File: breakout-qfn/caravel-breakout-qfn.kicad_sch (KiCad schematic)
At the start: 13 parts, among them CON1 REF-182665-01, CON2 REF-182665-01, CON3 73251-1352, U1 Caravel_QFN_TT4

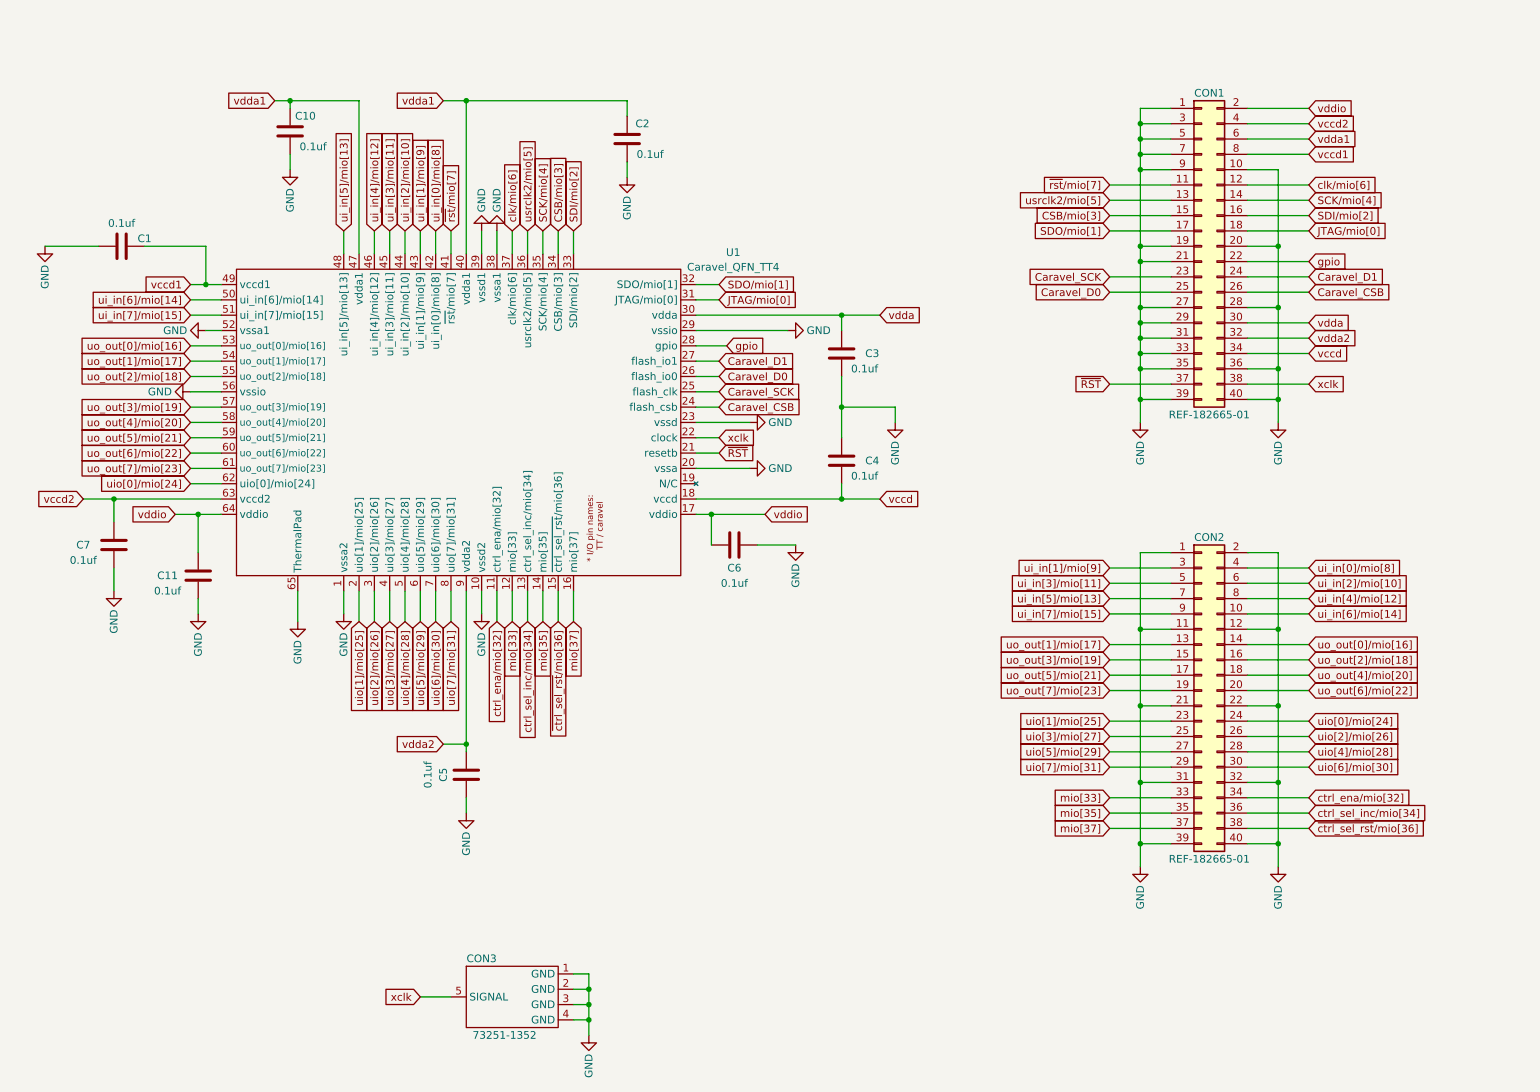
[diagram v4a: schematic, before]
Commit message: v3.0, breaking changes for ultra-goodness: EMC,TT pinout, FPGA
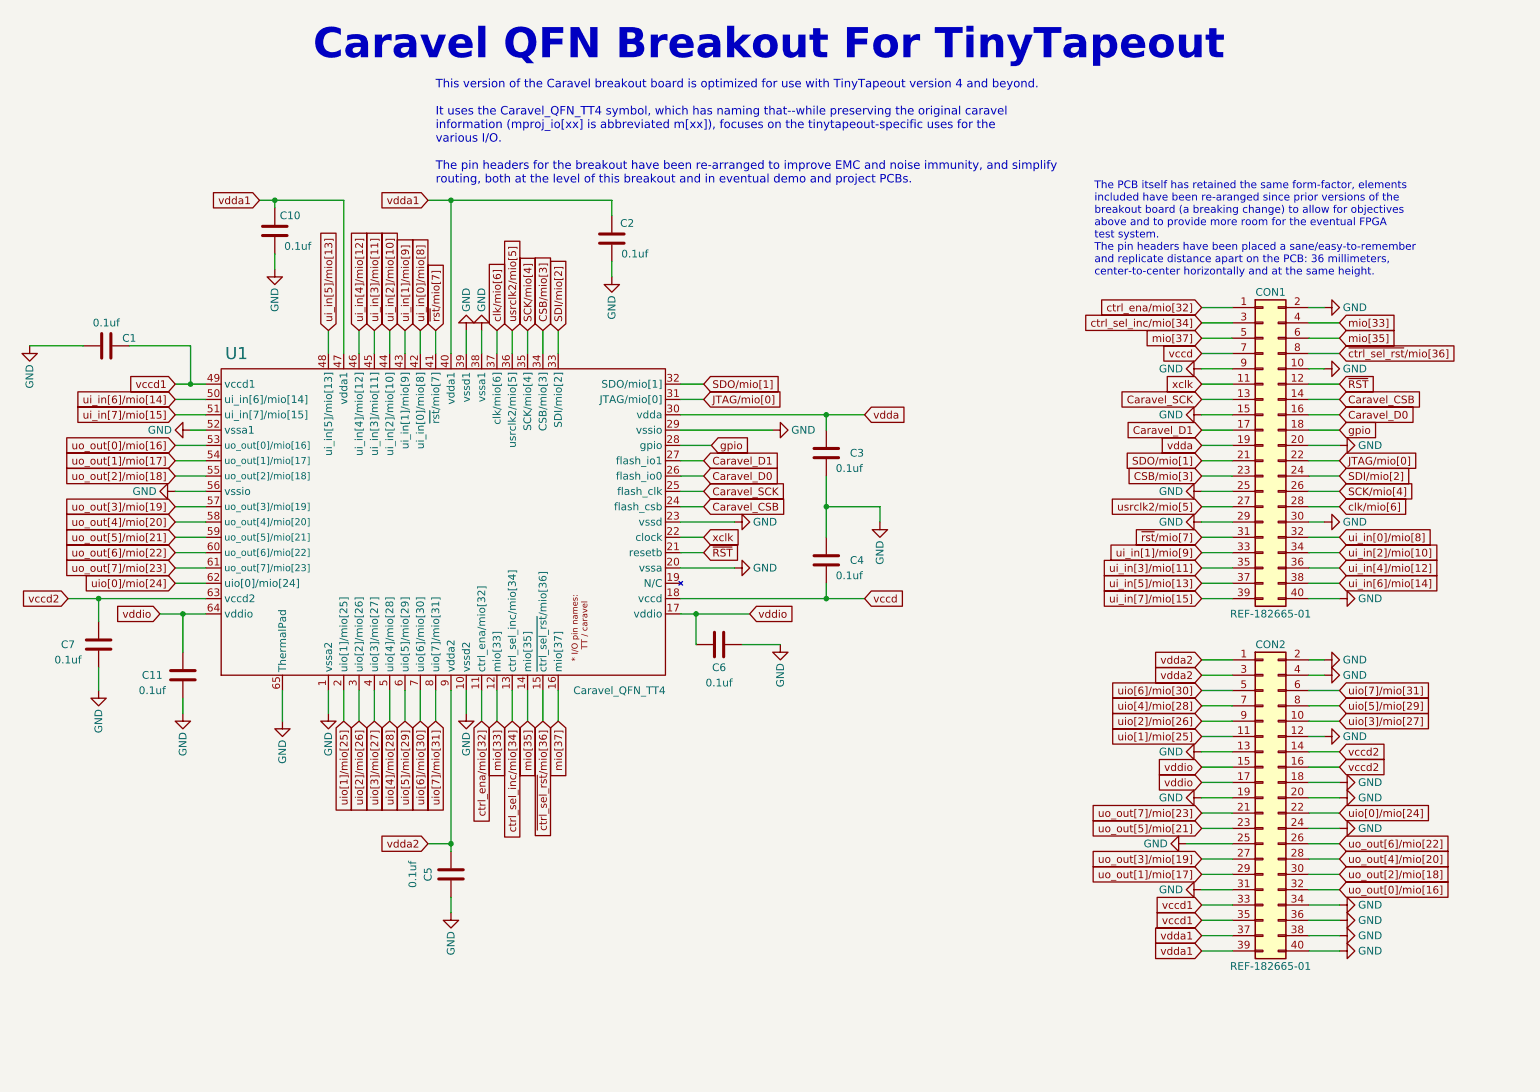
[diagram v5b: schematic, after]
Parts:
- removed CON3: 73251-1352, ok-connectors:TE_5-1814832-2, symbol ok-connectors:SMA_TH
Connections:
- net CSB/mio[3]: now also CON1.23 (Pin_23); no longer CON1.15 (Pin_15)
- net Caravel_CSB: now also CON1.14 (Pin_14); no longer CON1.26 (Pin_26)
- net Caravel_D0: now also CON1.16 (Pin_16); no longer CON1.25 (Pin_25)
- net Caravel_D1: now also CON1.17 (Pin_17); no longer CON1.24 (Pin_24)
- net Caravel_SCK: now also CON1.13 (Pin_13); no longer CON1.23 (Pin_23)
- net GND: now also CON1.15 (Pin_15), CON1.2 (Pin_2), CON1.25 (Pin_25), CON1.30 (Pin_30), CON2.13 (Pin_13), CON2.18 (Pin_18), CON2.19 (Pin_19), CON2.20 (Pin_20), CON2.24 (Pin_24), CON2.25 (Pin_25), CON2.34 (Pin_34), CON2.36 (Pin_36), CON2.38 (Pin_38), CON2.4 (Pin_4); no longer CON1.1 (Pin_1), CON1.19 (Pin_19), CON1.21 (Pin_21), CON1.27 (Pin_27), CON1.28 (Pin_28), CON1.3 (Pin_3), CON1.31 (Pin_31), CON1.33 (Pin_33), CON1.35 (Pin_35), CON1.36 (Pin_36), CON1.39 (Pin_39), CON1.5 (Pin_5), CON1.7 (Pin_7), CON2.1 (Pin_1), CON2.11 (Pin_11), CON2.21 (Pin_21), CON2.22 (Pin_22), CON2.32 (Pin_32), CON2.39 (Pin_39)
- net JTAG/mio[0]: now also CON1.22 (Pin_22); no longer CON1.18 (Pin_18)
- net SCK/mio[4]: now also CON1.26 (Pin_26); no longer CON1.14 (Pin_14)
- net SDI/mio[2]: now also CON1.24 (Pin_24); no longer CON1.16 (Pin_16)
- net SDO/mio[1]: now also CON1.21 (Pin_21); no longer CON1.17 (Pin_17)
- net clk/mio[6]: now also CON1.28 (Pin_28); no longer CON1.12 (Pin_12)
- net ctrl_ena/mio[32]: now also CON1.1 (Pin_1); no longer CON2.34 (Pin_34)
- net ctrl_sel_inc/mio[34]: now also CON1.3 (Pin_3); no longer CON2.36 (Pin_36)
- net gpio: now also CON1.18 (Pin_18); no longer CON1.22 (Pin_22)
- net mio[33]: now also CON1.4 (Pin_4); no longer CON2.33 (Pin_33)
- net mio[35]: now also CON1.6 (Pin_6); no longer CON2.35 (Pin_35)
- net mio[37]: now also CON1.5 (Pin_5); no longer CON2.37 (Pin_37)
- net ui_in[0]/mio[8]: now also CON1.32 (Pin_32); no longer CON2.4 (Pin_4)
- net ui_in[1]/mio[9]: now also CON1.33 (Pin_33); no longer CON2.3 (Pin_3)
- net ui_in[2]/mio[10]: now also CON1.34 (Pin_34); no longer CON2.6 (Pin_6)
- net ui_in[3]/mio[11]: now also CON1.35 (Pin_35); no longer CON2.5 (Pin_5)
- net ui_in[4]/mio[12]: now also CON1.36 (Pin_36); no longer CON2.8 (Pin_8)
- net ui_in[5]/mio[13]: now also CON1.37 (Pin_37); no longer CON2.7 (Pin_7)
- net ui_in[6]/mio[14]: now also CON1.38 (Pin_38); no longer CON2.10 (Pin_10)
- net ui_in[7]/mio[15]: now also CON1.39 (Pin_39); no longer CON2.9 (Pin_9)
- net uio[0]/mio[24]: now also CON2.22 (Pin_22); no longer CON2.24 (Pin_24)
- net uio[1]/mio[25]: now also CON2.11 (Pin_11); no longer CON2.23 (Pin_23)
- net uio[2]/mio[26]: now also CON2.9 (Pin_9); no longer CON2.26 (Pin_26)
- net uio[3]/mio[27]: now also CON2.10 (Pin_10); no longer CON2.25 (Pin_25)
- net uio[4]/mio[28]: now also CON2.7 (Pin_7); no longer CON2.28 (Pin_28)
- net uio[5]/mio[29]: now also CON2.8 (Pin_8); no longer CON2.27 (Pin_27)
- net uio[6]/mio[30]: now also CON2.5 (Pin_5); no longer CON2.30 (Pin_30)
- net uio[7]/mio[31]: now also CON2.6 (Pin_6); no longer CON2.29 (Pin_29)
- net uo_out[0]/mio[16]: now also CON2.32 (Pin_32); no longer CON2.14 (Pin_14)
- net uo_out[1]/mio[17]: now also CON2.29 (Pin_29); no longer CON2.13 (Pin_13)
- net uo_out[2]/mio[18]: now also CON2.30 (Pin_30); no longer CON2.16 (Pin_16)
- net uo_out[3]/mio[19]: now also CON2.27 (Pin_27); no longer CON2.15 (Pin_15)
- net uo_out[4]/mio[20]: now also CON2.28 (Pin_28); no longer CON2.18 (Pin_18)
- net uo_out[5]/mio[21]: now also CON2.23 (Pin_23); no longer CON2.17 (Pin_17)
- net uo_out[6]/mio[22]: now also CON2.26 (Pin_26); no longer CON2.20 (Pin_20)
- net uo_out[7]/mio[23]: now also CON2.21 (Pin_21); no longer CON2.19 (Pin_19)
- net usrclk2/mio[5]: now also CON1.27 (Pin_27); no longer CON1.13 (Pin_13)
- net vccd: now also CON1.7 (Pin_7); no longer CON1.34 (Pin_34)
- net vccd1: now also CON2.33 (Pin_33), CON2.35 (Pin_35); no longer CON1.8 (Pin_8)
- net vccd2: now also CON2.14 (Pin_14), CON2.16 (Pin_16); no longer CON1.4 (Pin_4)
- net vdda: now also CON1.19 (Pin_19); no longer CON1.30 (Pin_30)
- net vdda1: now also CON2.37 (Pin_37), CON2.39 (Pin_39); no longer CON1.6 (Pin_6)
- net vdda2: now also CON2.1 (Pin_1), CON2.3 (Pin_3); no longer CON1.32 (Pin_32)
- net vddio: now also CON2.15 (Pin_15), CON2.17 (Pin_17); no longer CON1.2 (Pin_2)
- net xclk: now also CON1.11 (Pin_11); no longer CON1.38 (Pin_38)
- net ~{RST}: now also CON1.12 (Pin_12); no longer CON1.37 (Pin_37)
- net ~{ctrl_sel_rst}/mio[36]: now also CON1.8 (Pin_8); no longer CON2.38 (Pin_38)
- net ~{rst}/mio[7]: now also CON1.31 (Pin_31); no longer CON1.11 (Pin_11)
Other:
- note added: "Caravel QFN Breakout For TinyTapeout"
- note added: "The PCB itself has retained the same form-factor, elements included have been re-aranged since prior versions of the breakout board (a breaking change) to allow for objectives above and to provide more room for the eventual FPGA test system. The pin headers have been placed a sane/easy-to-remember and replicate distance apart on the PCB: 36 millimeters, center-to-center horizontally and at the sa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"
- note added: "This version of the Caravel breakout board is optimized for use with TinyTapeout version 4 and beyond. It uses the Caravel_QFN_TT4 symbol, which has naming that--while preserving the original caravel information (mproj_io[xx] is abbreviated m[xx]), focuses on the tinytapeout-specific uses for the various I/O. The pin headers for the breakout have been re-arranged to improve EMC and noise immunity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"
- company: (none) -> Psychogenic Technologies
- moved on the sheet: C1, C10, C11, C2, C3, C4, C5, C6, C7, CON1, CON2, U1

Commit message: Comments and cleanup
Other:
- note added: "Caravel CLK"
- note added: "Caravel CLK and ~{RST}"
- note added: "Caravel flash"
- note added: "Caravel ~{RST}"
- note added: "HK SPI"
- note added: "Inputs"
- note added: "MUX Control"
- note added: "Project CLK"
- note added: "Project ~{RST}"
- note added: "This version of the Caravel breakout board is optimized for use with TinyTapeout version 4 and beyond. It uses the Caravel_QFN_TT4 symbol, which has naming that--while preserving the original caravel information (mproj_io[xx] is abbreviated m[xx])--focuses on the tinytapeout-specific uses for the various I/O. The pin headers for the breakout have been re-arranged to improve EMC and noise immunity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"
- note added: "Though the PCB itself has retained the same form-factor, elements included have been re-aranged since prior versions of the breakout board (a breaking change) to allow for objectives above and to provide more room for the eventual FPGA test system. The pin headers have been placed a sane/easy-to-remember and replicate distance apart on the PCB: 36 millimeters, center-to-center horizontally and at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"
- note added: "bidirectionals"
- note added: "caravel flash"
- note added: "outputs"
- note removed: "The PCB itself has retained the same form-factor, elements included have been re-aranged since prior versions of the breakout board (a breaking change) to allow for objectives above and to provide more room for the eventual FPGA test system. The pin headers have been placed a sane/easy-to-remember and replicate distance apart on the PCB: 36 millimeters, center-to-center horizontally and at the sa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"
- note removed: "This version of the Caravel breakout board is optimized for use with TinyTapeout version 4 and beyond. It uses the Caravel_QFN_TT4 symbol, which has naming that--while preserving the original caravel information (mproj_io[xx] is abbreviated m[xx]), focuses on the tinytapeout-specific uses for the various I/O. The pin headers for the breakout have been re-arranged to improve EMC and noise immunity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"
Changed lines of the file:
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@@
     (effects (font (size 5 5) (thickness 1) bold) (justify left bottom))
   )
-  (text "The PCB itself has retained the same form-factor, elements\nincluded have been re-aranged since prior versions of the \nbreakout board (a breaking change) to allow for objectives\nabove and to provide more room for the eventual FPGA \ntest system.  \nThe pin headers have been placed a sane/easy-to-remember \nand replicate distance apart on the PCB: 36 millimeters, \ncenter-to-center horizontally and at the same height."
+  (text "Project\nCLK" (at 97.79 52.07 90)
+    (effects (font (size 1 1)) (justify left bottom))
+  )
+  (text "MUX\nControl" (at 190.5 65.405 90)
+    (effects (font (size 1 1)) (justify left bottom))
+  )
+  (text "Caravel CLK" (at 196.85 74.295 0)
+    (effects (font (size 1 1)) (justify left bottom))
+  )
+  (text "HK SPI" (at 101.6 50.8 0)
+    (effects (font (size 1.27 1.27)) (justify left bottom))
+  )
+  (text "HK SPI" (at 252.095 92.71 90)
+    (effects (font (size 1.27 1.27)) (justify left bottom))
+  )
+  (text "outputs" (at 257.81 151.765 90)
+    (effects (font (size 1 1)) (justify right bottom))
+  )
+  (text "HK SPI" (at 144.78 74.93 0)
+    (effects (font (size 1.27 1.27)) (justify left bottom))
+  )
+  (text "outputs" (at 192.405 148.59 90)
+    (effects (font (size 1 1)) (justify right bottom))
+  )
+  (text "Project ~{RST}" (at 191.135 99.695 0)
+    (effects (font (size 1 1)) (justify left bottom))
+  )
+  (text "Caravel flash" (at 249.555 79.375 0)
+    (effects (font (size 1 1)) (justify left bottom))
+  )
+  (text "Project CLK" (at 248.92 95.25 0)
+    (effects (font (size 1 1)) (justify left bottom))
+  )
+  (text "Though the PCB itself has retained the same form-factor, \nelements included have been re-aranged since prior versions \nof the breakout board (a breaking change) to allow for \nobjectives above and to provide more room for the eventual \nFPGA test system.  \nThe pin headers have been placed a sane/easy-to-remember \nand replicate distance apart on the PCB: 36 millimeters, \ncenter-to-center horizontally and at the same height."
     (at 195.58 55.88 0)
     (effects (font (size 1.27 1.27)) (justify left bottom))
   )
-  (text "This version of the Caravel breakout board is optimized for use with TinyTapeout version 4 and beyond.\n\nIt uses the Caravel_QFN_TT4 symbol, which has naming that--while preserving the original caravel \ninformation (mproj_io[xx] is abbreviated m[xx]), focuses on the tinytapeout-specific uses for the\nvarious I/O.\n\nThe pin headers for the breakout have been re-arranged to improve EMC and noise immunity, and simplify\nrouting, both at the level of this breakout and in eventual demo and project PCBs."
+  (text "Caravel ~{RST}" (at 242.57 74.295 0)
+    (effects (font (size 1 1)) (justify left bottom))
+  )
+  (text "Inputs" (at 194.31 107.95 90)
+    (effects (font (size 1 1)) (justify left bottom))
+  )
+  (text "bidirectionals" (at 195.58 133.985 90)
+    (effects (font (size 1 1)) (justify left bottom))
+  )
+  (text "Caravel\nCLK and ~{RST}" (at 137.16 101.6 0)
+    (effects (font (size 1 1)) (justify left bottom))
+  )
+  (text "Project\n~{RST}" (at 88.265 52.07 90)
+    (effects (font (size 1 1)) (justify left bottom))
+  )
+  (text "This version of the Caravel breakout board is optimized for use with TinyTapeout version 4 and beyond.\n\nIt uses the Caravel_QFN_TT4 symbol, which has naming that--while preserving the original caravel \ninformation (mproj_io[xx] is abbreviated m[xx])--focuses on the tinytapeout-specific uses for the\nvarious I/O.\n\nThe pin headers for the breakout have been re-arranged to improve EMC and noise immunity, and \nsimplify routing, both at the level of this breakout and in eventual demo and project PCBs."
     (at 86.36 40.64 0)
     (effects (font (size 1.4 1.4)) (justify left bottom))
   )
+  (text "caravel flash" (at 147.32 96.52 90)
+    (effects (font (size 1.27 1.27)) (justify left bottom))
+  )
   (global_label "JTAG{slash}mio[0]" (shape input) (at 236.22 86.36 0) (fields_autoplaced)
